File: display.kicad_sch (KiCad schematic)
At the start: 14 parts, among them U3 SSD1306

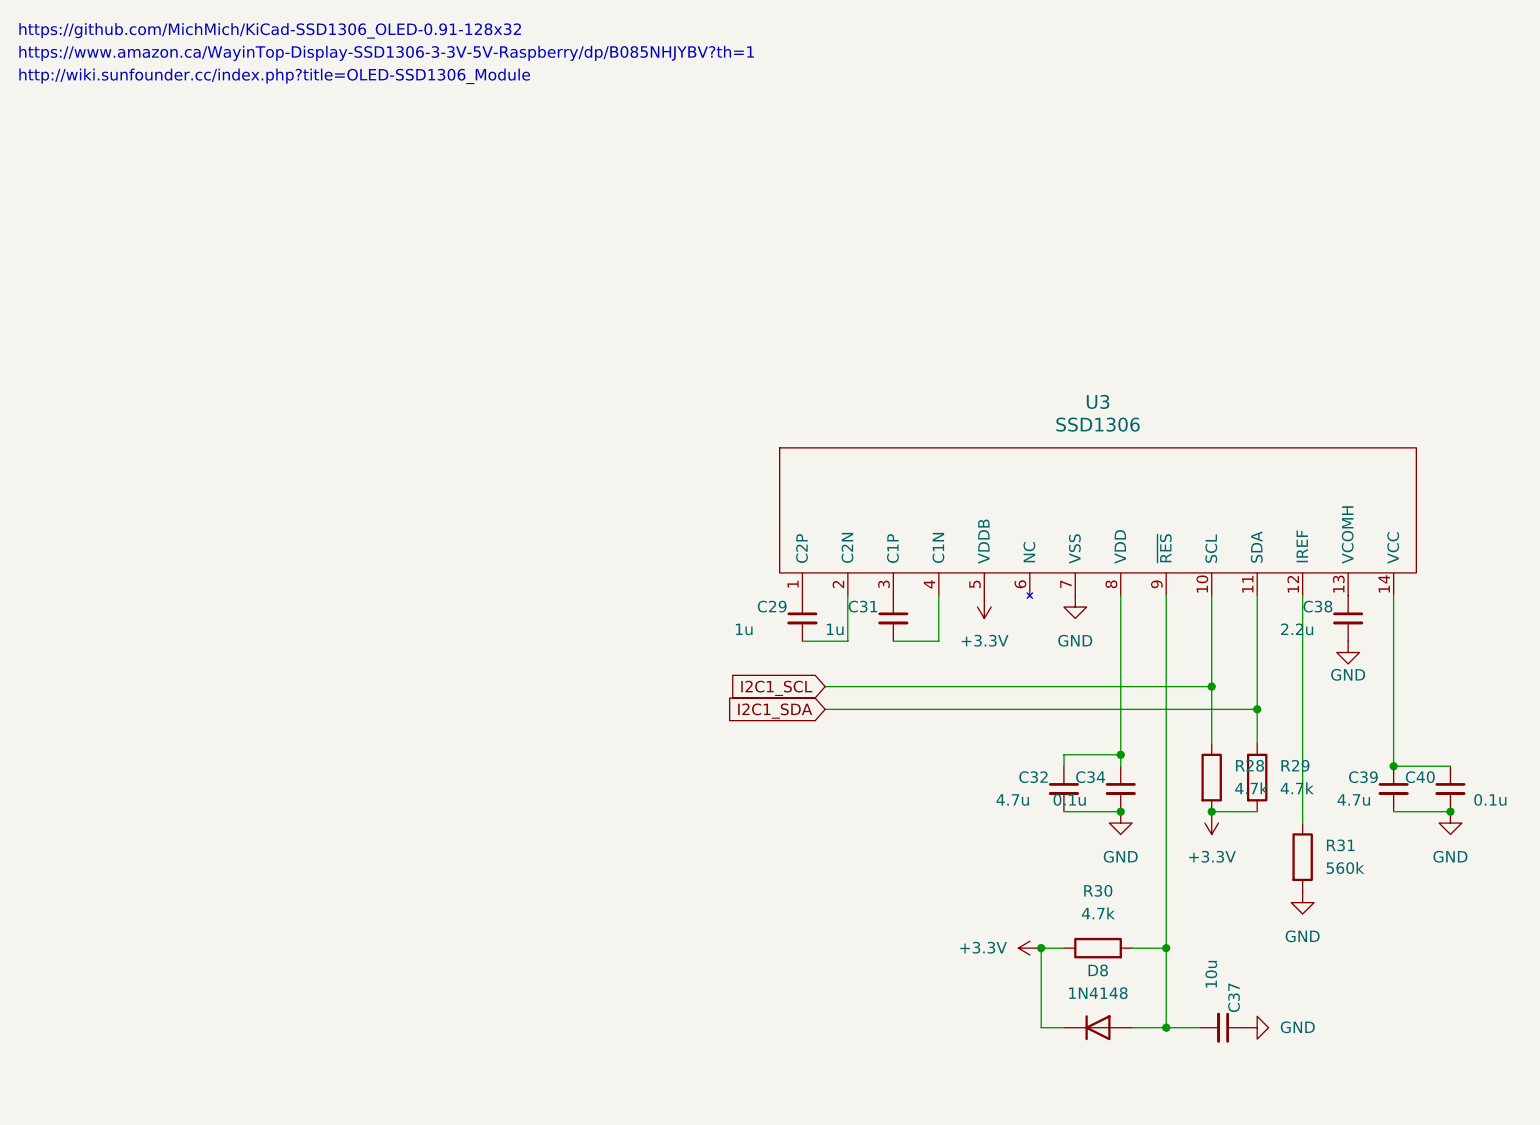
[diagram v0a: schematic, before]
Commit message: Add USB circuit (peripheral mode only)
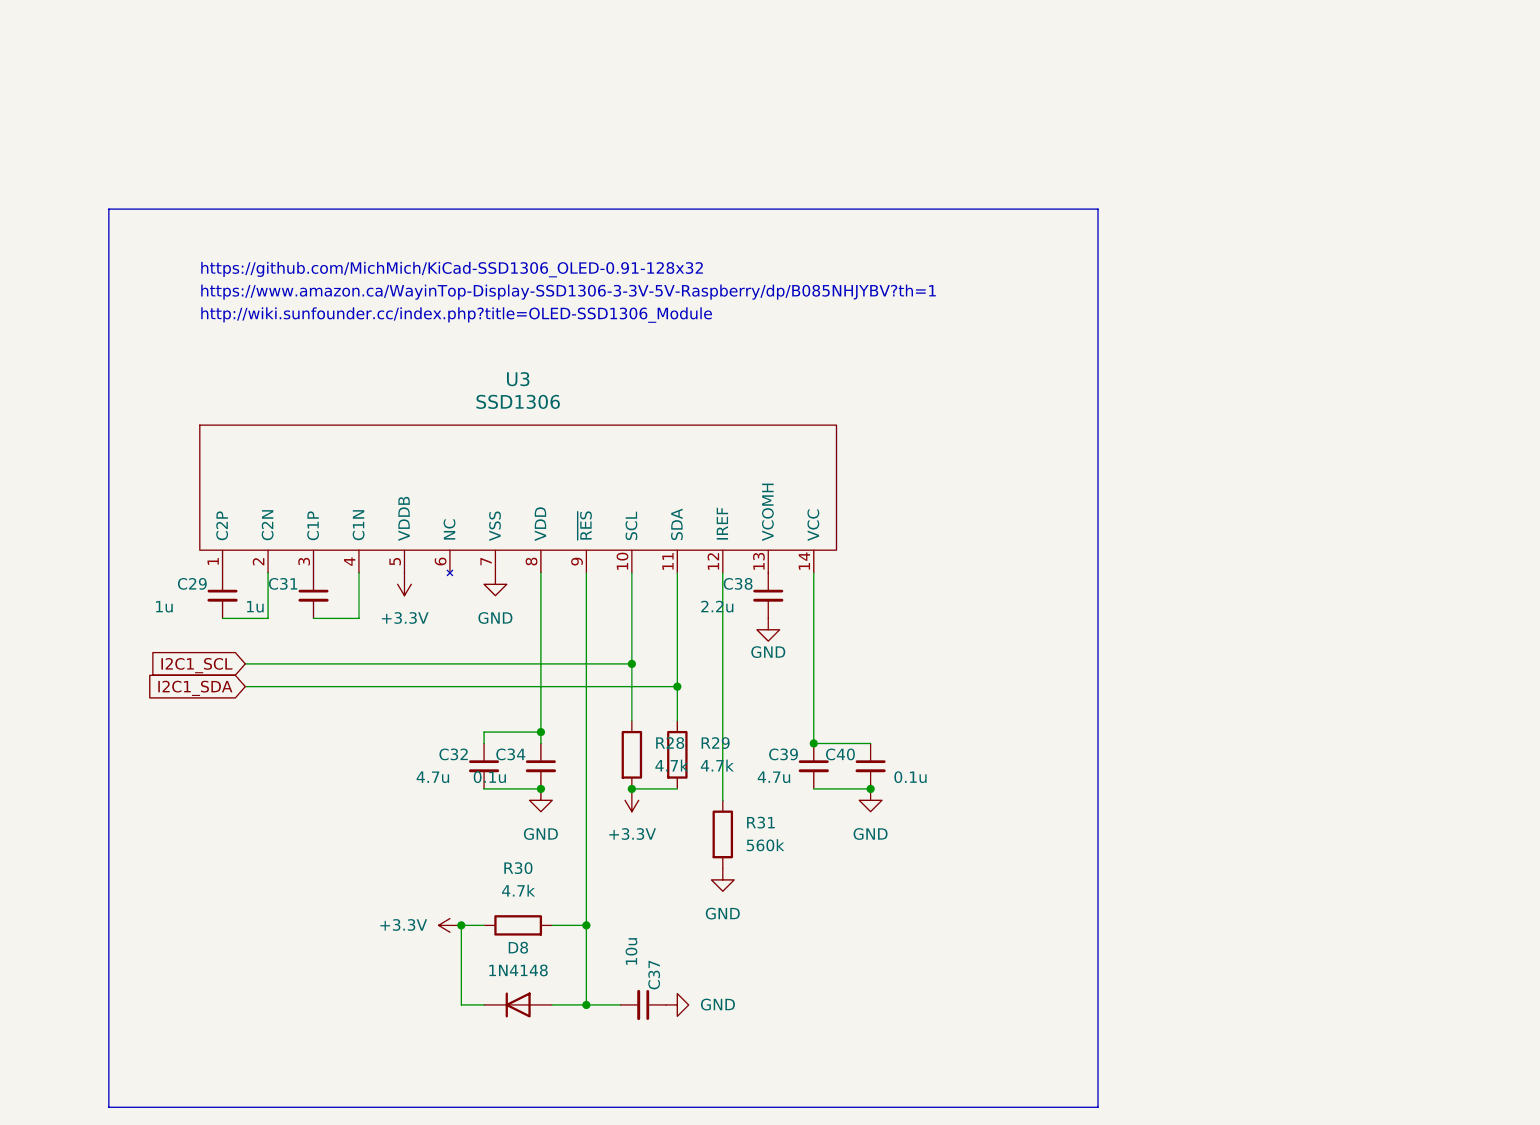
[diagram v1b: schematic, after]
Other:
- moved on the sheet: C29, C31, C32, C34, C37, C38, C39, C40, D8, R28, R29, R30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
